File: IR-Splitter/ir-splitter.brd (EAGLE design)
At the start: 80 x 100 mm, 33 parts, among them T1 IRFR024N, T10 IRFR024N, T2 IRFR024N, T3 IRFR024N, T4 IRFR024N, T5 IRFR024N, T6 IRFR024N, T7 IRFR024N, T8 IRFR024N, T9 IRFR024N, X1 250-202

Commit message: Updated IR-Splitter
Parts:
- removed JP1, JP2: (no value), pinhead:1X04/90
- removed LED1: (no value), led:LED5MM
- removed PAD1: IR-IN-DATA, wirepad:3,81/1,4
- removed PAD3: IR-IN-GND, wirepad:3,81/1,4
- removed R2: 300R, rcl:0207/15
- removed SUPPLY_OUT: (no value), wirepad:3,81/1,4
- added GND: IR-IN-GND, wirepad:3,81/1,4
- added IR_DATA: IR-IN-DATA, wirepad:3,81/1,4
- renumbered X1 to SUPPLY
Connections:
- removed net N$1: LED1.A, R2.1
- net +12V: no longer JP1.2, JP1.3, JP2.2, JP2.3, R2.2, SUPPLY_OUT.1
- net GND: now also GND.1; no longer JP1.1, JP1.4, JP2.1, JP2.4, PAD3.1
- net IR-IN-DATA: now also IR_DATA.1; no longer LED1.K, PAD1.1
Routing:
- net +12V: track 133.6 -> 8.02 mm
- net GND: track 82.9 -> 192.1 mm
- net IR-IN-DATA: track 166.1 -> 219.6 mm
- net N$1: track 5.61 -> 0.00 mm
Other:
- board text added: "NorthernStars IR-Splitter v0.0.1"
- board text removed: "DATA"
- board text removed: "IR-Splitter v0.1"
- board text removed: "NorthernStars"

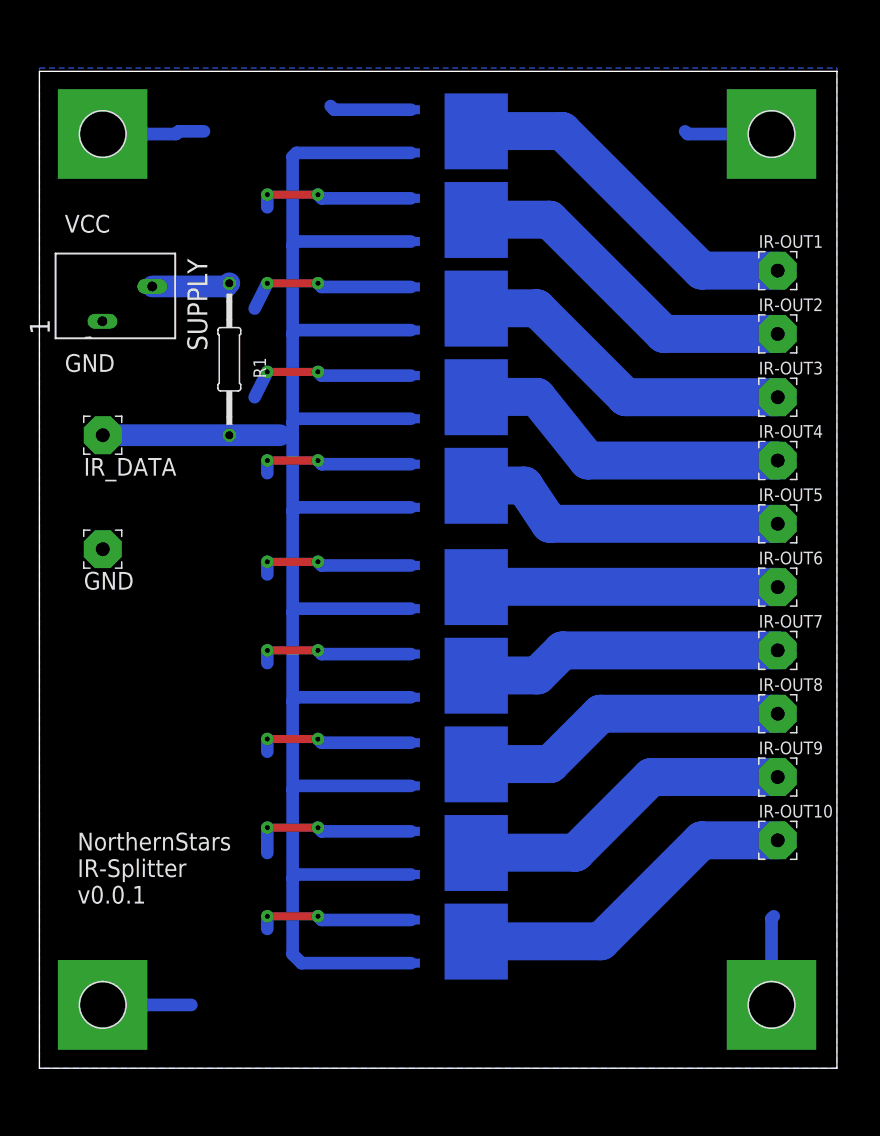
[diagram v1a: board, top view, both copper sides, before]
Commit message: Updated IR Splitter schematics and layout to avoid damage of IR leds
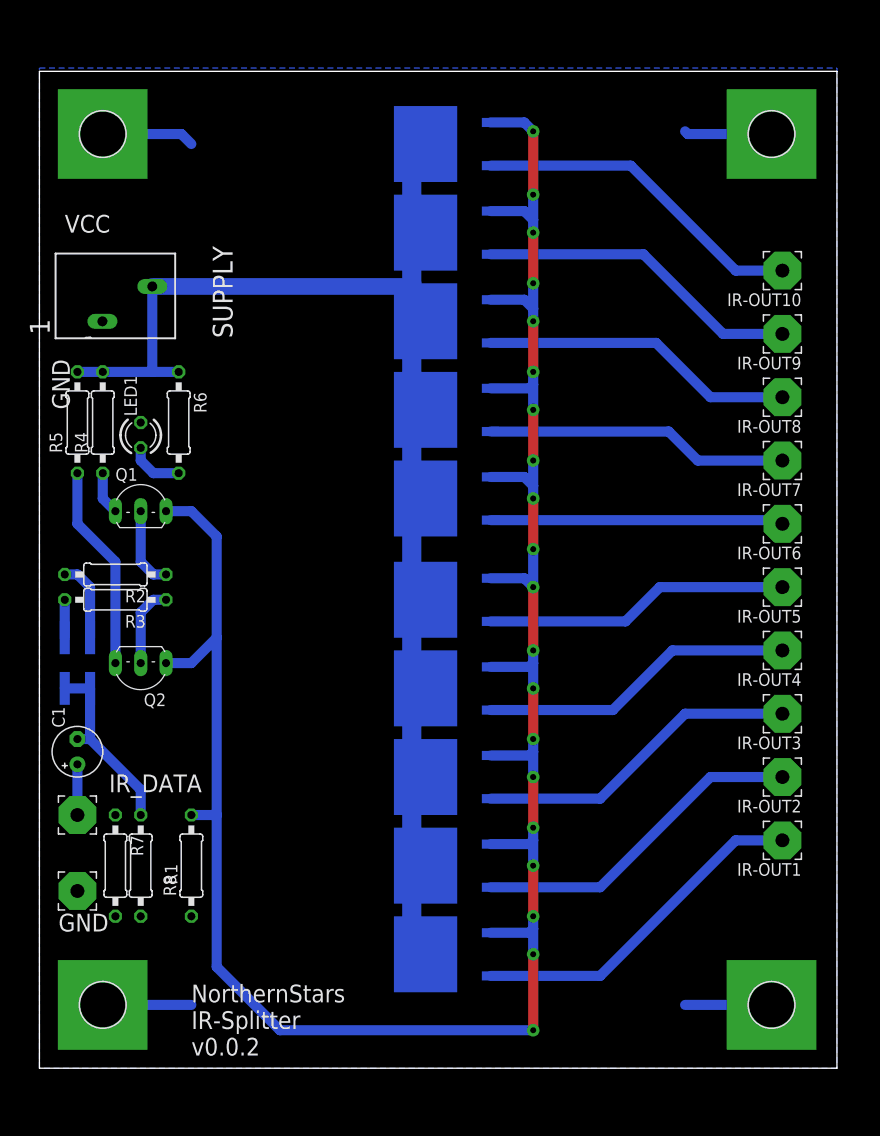
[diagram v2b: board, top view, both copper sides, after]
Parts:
- added C1: (no value), rcl:E2,5-5
- added JP1: (no value), pinhead-2:2X02SMD
- added LED1: (no value), led:LED3MM
- added Q1: BC447, transistor-npn:TO92-EBC
- added Q2: BC557B, transistor-pnp:TO92-EBC
- added R2, R3: 1k5, rcl:0207/10
- added R4, R5, R7, R8: 1k, rcl:0207/10
- added R6: 330R, rcl:0207/10
- R1: value 1k -> 10k; device rcl:0207/15 -> rcl:0207/10
- moved T1 82.6 mm to (40.2, 11.4), turned to 270 degrees
- moved T10 80.0 mm to (40.2, 92.7), turned to 270 degrees
- moved T2 64.8 mm to (40.2, 20.3), turned to 270 degrees
- moved T9 62.3 mm to (40.2, 83.8), turned to 270 degrees
- moved IR-OUT1 57.2 mm to (74.5, 22.9), turned to 180 degrees
- moved IR-OUT10 57.2 mm to (74.5, 80.0), turned to 180 degrees
- moved R1 51.6 mm to (10.2, 20.3)
- moved T3 47.0 mm to (40.2, 29.2), turned to 270 degrees
- moved T8 44.5 mm to (40.2, 74.9), turned to 270 degrees
- moved IR-OUT2 44.5 mm to (74.5, 29.2), turned to 180 degrees
- moved IR-OUT9 44.5 mm to (74.5, 73.7), turned to 180 degrees
- moved IR_DATA 38.2 mm to (3.81, 25.4)
- moved GND 34.4 mm to (3.81, 17.8)
- moved IR-OUT3 31.8 mm to (74.5, 35.6), turned to 180 degrees
- moved IR-OUT8 31.8 mm to (74.5, 67.3), turned to 180 degrees
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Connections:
- removed net +12V: R1.2, SUPPLY.L2
- removed net IR-IN-DATA: IR_DATA.1, R1.1, T1.G, T10.G, T2.G, T3.G, T4.G, T5.G, T6.G, T7.G, T8.G, T9.G
- new net DATA: C1.-, JP1.2, JP1.4, R1.2
- new net IR-DATA: Q1.E, Q2.C, R8.2, T1.G, T10.G, T2.G, T3.G, T4.G, T5.G, T6.G, T7.G, T8.G, T9.G
- new net N$1: IR-OUT1.1, T1.S
- new net N$12: Q1.C, R4.1
- new net N$13: Q2.E, R5.1
- new net N$14: Q2.B, R3.1
- new net N$15: LED1.A, R6.2
- new net N$16: C1.+, IR_DATA.1, R7.2
- new net N$17: JP1.3, R2.2
- new net N$18: JP1.1, R3.2
- new net VCC: R4.2, R5.2, R6.1, SUPPLY.L2, T1.D, T10.D, T2.D, T3.D, T4.D, T5.D, T6.D, T7.D, T8.D, T9.D
- net GND: now also LED1.K, R1.1, R7.1, R8.1; no longer T1.S, T10.S, T2.S, T3.S, T4.S, T5.S, T6.S, T7.S, T8.S, T9.S
- net N$10: now also T9.S; no longer T9.D
- net N$11: now also Q1.B, R2.1; no longer IR-OUT10.1, T10.D
- net N$2: now also IR-OUT2.1, T2.S; no longer IR-OUT1.1, T1.D
- net N$3: now also IR-OUT5.1, T5.S; no longer IR-OUT2.1, T2.D
- net N$4: now also IR-OUT6.1, T6.S; no longer IR-OUT3.1, T3.D
- net N$5: now also IR-OUT8.1, T8.S; no longer IR-OUT4.1, T4.D
- net N$6: now also IR-OUT7.1, T7.S; no longer IR-OUT5.1, T5.D
- net N$7: now also IR-OUT4.1, T4.S; no longer IR-OUT6.1, T6.D
- net N$8: now also IR-OUT3.1, T3.S; no longer IR-OUT7.1, T7.D
- net N$9: now also IR-OUT10.1, T10.S; no longer IR-OUT8.1, T8.D
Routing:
- net IR-DATA: track 0.00 -> 227.8 mm, vias 0 -> 20
- net IR-IN-DATA: track 219.6 -> 0.00 mm
- net GND: track 192.1 -> 35.6 mm, vias 18 -> 0
- net VCC: track 0.00 -> 126.2 mm
- net N$1: track 0.00 -> 34.9 mm
- net N$11: track 33.1 -> 8.15 mm
- net N$13: track 0.00 -> 20.6 mm
- net DATA: track 0.00 -> 18.6 mm
- net N$17: track 0.00 -> 8.15 mm
- net N$14: track 0.00 -> 8.15 mm
- net +12V: track 8.02 -> 0.00 mm
- net N$15: track 0.00 -> 5.61 mm
- net N$16: track 0.00 -> 5.08 mm
- net N$12: track 0.00 -> 4.34 mm
- net N$18: track 0.00 -> 3.81 mm
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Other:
- board text added: "NorthernStars IR-Splitter v0.0.2"
- board text removed: "NorthernStars IR-Splitter v0.0.1"

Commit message: Updated IR-Splitter to Version 1.0.0
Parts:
- removed C1: (no value), rcl:E2,5-5
- removed JP1: (no value), pinhead-2:2X02SMD
- added R10, R11, R12, R13, R14, R9: >100k, rcl:R1206
- LED1: device led:LED3MM -> led:CHIPLED_1206
- Q1: value BC447 -> BC548B
- Q2: value BC557B -> BC548B; device transistor-pnp:TO92-EBC -> transistor-npn:TO92-EBC
- R1: value 10k -> 1k; device rcl:0207/10 -> rcl:R1206
- R2, R3: value 1k5 -> 1k; device rcl:0207/10 -> rcl:R1206
- R4, R5, R7, R8: value 1k -> >100k; device rcl:0207/10 -> rcl:R1206
- R6: device rcl:0207/10 -> rcl:R1206
- moved R4 72.8 mm to (55.9, 11.4), flipped to the bottom, turned to 270 degrees
- moved R5 68.5 mm to (55.9, 20.3), flipped to the bottom, turned to 270 degrees
- moved R7 49.1 mm to (55.9, 29.2), flipped to the bottom
- moved R8 44.4 mm to (55.9, 38.1), flipped to the bottom, turned to 270 degrees
- moved R1 32.0 mm to (6.35, 52.1), flipped to the bottom, turned to 0 degrees
- moved R2 20.4 mm to (6.35, 29.2), flipped to the bottom, turned to 0 degrees
- moved Q1 18.0 mm to (7.62, 39.4)
- moved R3 12.0 mm to (19.1, 50.8), flipped to the bottom, turned to 270 degrees
- moved Q2 10.5 mm to (7.62, 49.5), turned to 0 degrees
- moved R6 5.24 mm to (12.7, 69.8), flipped to the bottom, turned to 180 degrees
- moved GND 3.81 mm to (7.62, 17.8)
- moved IR_DATA 3.81 mm to (7.62, 25.4)
- moved LED1 3.59 mm to (12.7, 66.0), flipped to the bottom, turned to 270 degrees
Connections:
- removed net DATA: C1.-, JP1.2, JP1.4, R1.2
- removed net N$12: Q1.C, R4.1
- removed net N$13: Q2.E, R5.1
- removed net N$14: Q2.B, R3.1
- removed net N$17: JP1.3, R2.2
- removed net N$18: JP1.1, R3.2
- net GND: now also LED1.C, Q1.E, R10.1, R11.1, R12.1, R13.1, R14.1, R3.1, R4.1, R5.1, R9.1; no longer LED1.K, R1.1
- net IR-DATA: now also Q2.E, R3.2; no longer Q1.E, Q2.C, R8.2
- net N$1: now also R4.2
- net N$10: now also R12.2
- net N$11: now also Q1.C, Q2.B, R1.1; no longer Q1.B, R2.1
- net N$16: now also Q1.B, R2.1; no longer C1.+, R7.2
- net N$2: now also R5.2
- net N$3: now also R14.2
- net N$4: now also R11.2
- net N$5: now also R9.2
- net N$6: now also R10.2
- net N$7: now also R8.2
- net N$8: now also R7.2
- net N$9: now also R13.2
- net VCC: now also Q2.C, R1.2, R2.2; no longer R4.2, R5.2
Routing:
- net VCC: track 126.2 -> 165.0 mm
- net N$13: track 20.6 -> 0.00 mm
- net DATA: track 18.6 -> 0.00 mm
- net IR-DATA: track 227.8 -> 215.9 mm
- net N$17: track 8.15 -> 0.00 mm
- net N$14: track 8.15 -> 0.00 mm
- net N$16: track 5.08 -> 12.8 mm
- net N$11: track 8.15 -> 15.1 mm
- net N$12: track 4.34 -> 0.00 mm
- net N$18: track 3.81 -> 0.00 mm
- net N$15: track 5.61 -> 3.95 mm
- net N$8: track 32.8 -> 33.5 mm
- net N$2: track 33.8 -> 34.6 mm
- net N$7: track 31.7 -> 32.5 mm
- net N$3: track 30.7 -> 31.4 mm
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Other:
- board text added: "NorthernStars IR-Splitter v1.0.0"
- board text removed: "NorthernStars IR-Splitter v0.0.2"
